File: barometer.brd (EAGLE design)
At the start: 58.4 x 40.4 mm, 95 parts, among them IC1 MIC5225-3.3v, IC2 TPS5410, IC3 ZPA2326-0311A-R, U1 MCP4725A0, U2 LTC2850, U3 PCA9306, U4 MAX3221, U5 XC6215XC6215B182NR, U6 Tiny85-20-SMT, X2 1751264, X3 1751248

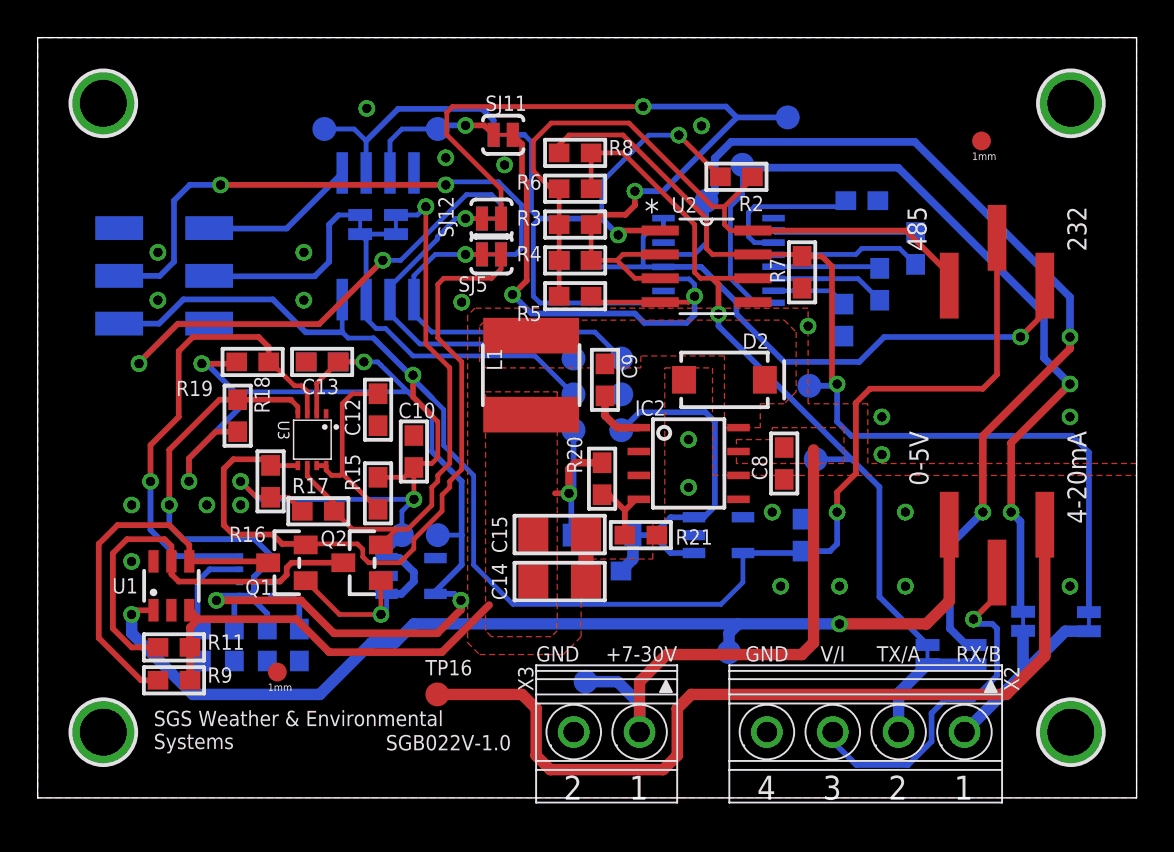
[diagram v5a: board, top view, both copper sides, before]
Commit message: Add 0-5 V to 4-20 mA converter
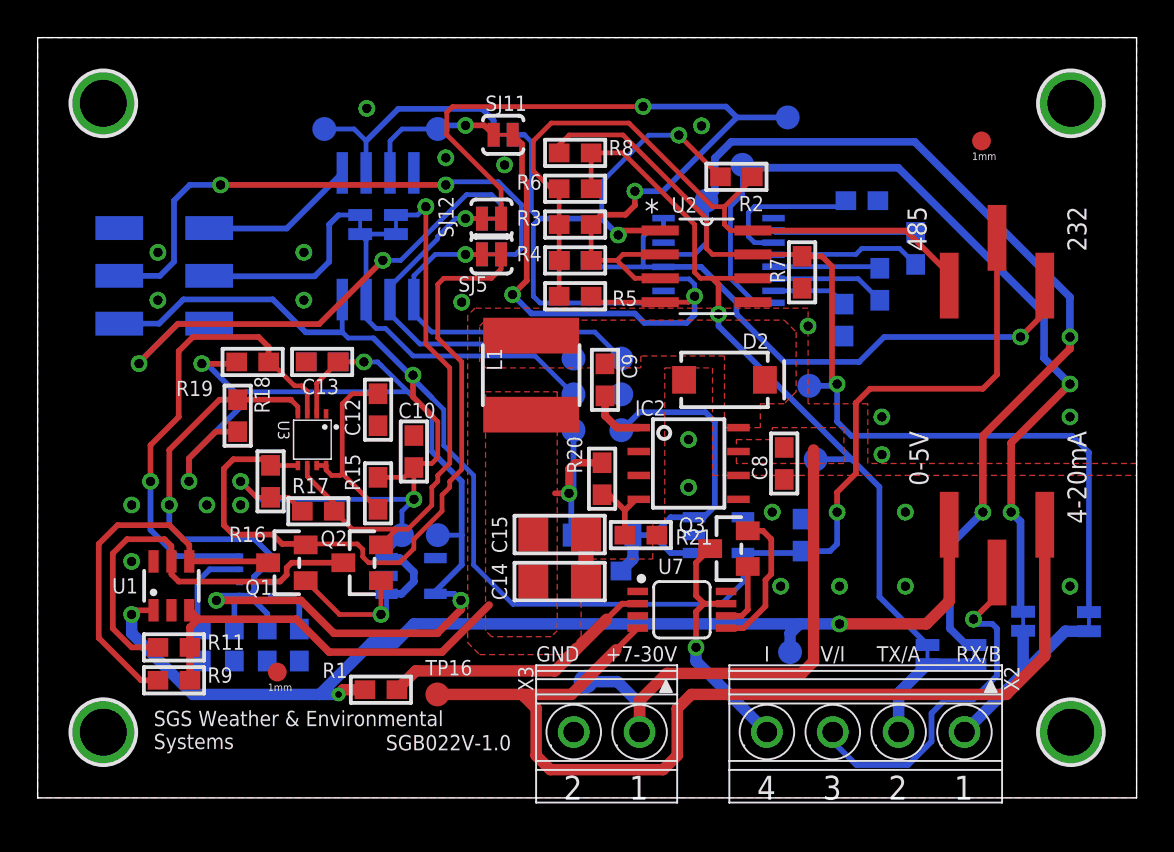
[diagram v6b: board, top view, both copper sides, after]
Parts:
- added Q3: BC817, microbuilder:SOT23-WIDE
- added R1: 25k, microbuilder:0603
- added U7: XTR117, transceiver-burrbrown:MSOP8-0.65-3X3MM
- moved TP15 3.25 mm to (40.0, 7.75)
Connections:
- new net BASE: Q3.1, U7.6
- new net COLLECTOR: Q3.3, U7.7, X2.4
- new net EMITTER: Q3.2, U7.5
- new net I-IN: R1.1, U7.2
- net GND: now also U7.3; no longer X2.4
- net I-OUT: now also U7.4
- net V-OUT: now also R1.2
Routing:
- net I-IN: track 0.00 -> 14.7 mm
- net COLLECTOR: track 0.00 -> 13.1 mm, vias 0 -> 1
- net EMITTER: track 0.00 -> 7.70 mm
- net I-OUT: track 46.4 -> 54.0 mm
- net BASE: track 0.00 -> 3.58 mm
- net V-OUT: track 54.9 -> 57.4 mm, vias 2 -> 3
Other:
- board text added: "I"
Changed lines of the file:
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@@
 <text x="34" y="7.25" size="0.8128" layer="25" font="vector" ratio="18" align="bottom-right">+7-30V</text>
 <text x="26.5" y="7.25" size="0.8128" layer="25" font="vector" ratio="18">GND</text>
-<text x="38.77" y="7.25" size="0.8128" layer="25" font="vector" ratio="18" align="bottom-center">GND</text>
+<text x="38.77" y="7.25" size="0.8128" layer="25" font="vector" ratio="18" align="bottom-center">I</text>
 <text x="51.23" y="7.25" size="0.8128" layer="25" font="vector" ratio="18" align="bottom-right">RX/B</text>
 <text x="45.77" y="7.25" size="0.8128" layer="25" font="vector" ratio="18" align="bottom-center">TX/A</text>
@@
 </element>
 <element name="R5" library="microbuilder" package="0603" value="10k" x="28.575" y="26.6675" smashed="yes" rot="R180">
-<attribute name="NAME" x="26.797" y="26.1595" size="0.8128" layer="25" font="vector" ratio="18" rot="R180"/>
+<attribute name="NAME" x="30.547" y="26.1595" size="0.8128" layer="25" font="vector" ratio="18"/>
 </element>
 <element name="R6" library="microbuilder" package="0603" value="20k" x="28.575" y="32.3825" smashed="yes" rot="R180">
@@
 <attribute name="NAME" x="23.7975" y="36.52" size="0.8128" layer="25" font="vector" ratio="18"/>
 </element>
-<element name="TP15" library="testpad" library_urn="urn:adsk.eagle:library:385" package="B1,27" package3d_urn="urn:adsk.eagle:package:27944/1" value="PTR1B1,27" x="36.75" y="7.75" smashed="yes" rot="MR0">
-<attribute name="NAME" x="38.385" y="8.766" size="0.8128" layer="26" font="vector" ratio="18" rot="MR0"/>
-<attribute name="TP_SIGNAL_NAME" value="" x="37.385" y="5.845" size="1" layer="38" rot="MR0"/>
+<element name="TP15" library="testpad" library_urn="urn:adsk.eagle:library:385" package="B1,27" package3d_urn="urn:adsk.eagle:package:27944/1" value="PTR1B1,27" x="40" y="7.75" smashed="yes" rot="MR0">
+<attribute name="NAME" x="41.635" y="8.766" size="0.8128" layer="26" font="vector" ratio="18" rot="MR0"/>
+<attribute name="TP_SIGNAL_NAME" value="" x="40.635" y="5.845" size="1" layer="38" rot="MR0"/>
 </element>
 <element name="TP16" library="testpad" library_urn="urn:adsk.eagle:library:385" package="B1,27" package3d_urn="urn:adsk.eagle:package:27944/1" value="PTR1B1,27" x="21.25" y="5.5" smashed="yes">
@@
 <attribute name="NAME" x="15.75" y="13.8" size="0.8128" layer="25" font="vector" ratio="18" rot="R180" align="center"/>
 <attribute name="VALUE" x="17.885" y="14.405" size="0.4064" layer="27" ratio="10" rot="R90"/>
+</element>
+<element name="U7" library="transceiver-burrbrown" package="MSOP8-0.65-3X3MM" value="XTR117" x="34.25" y="10" smashed="yes">
+<attribute name="NAME" x="32.98" y="11.905" size="0.8128" layer="25" font="vector" ratio="18"/>
+</element>
+<element name="R1" library="microbuilder" package="0603" value="25k" x="18.25" y="5.75" smashed="yes" rot="R180">
+<attribute name="NAME" x="16.472" y="6.377" size="0.8128" layer="25" font="vector" ratio="18" rot="R180" align="top-left"/>
+</element>
+<element name="Q3" library="microbuilder" package="SOT23-WIDE" value="BC817" x="36.75" y="13.25" smashed="yes" rot="R90">
+<attribute name="NAME" x="35.5" y="14.905" size="0.8128" layer="25" font="vector" ratio="18" rot="R180"/>
 </element>
 </elements>
@@
 <via x="5" y="15.57" extent="1-16" drill="0.5"/>
 <contactref element="X3" pad="2"/>
-<contactref element="X2" pad="4"/>
 <via x="10.795" y="15.57" extent="1-16" drill="0.5"/>
 <via x="14.1525" y="28.9975" extent="1-16" drill="0.5"/>
@@
 <via x="5" y="12.57" extent="1-16" drill="0.5"/>
 <via x="9" y="15.57" extent="1-16" drill="0.5"/>
+<contactref element="U7" pad="3"/>
 </signal>
 <signal name="+5V0">
@@
 <vertex x="37.1475" y="17.7775"/>
 </polygon>
-<wire x1="32" y1="6.1775" x2="33.44" y2="7.6175" width="0.6096" layer="1"/>
+<wire x1="32" y1="5.1775" x2="33.44" y2="6.6175" width="0.6096" layer="1"/>
 <contactref element="X3" pad="1"/>
-<wire x1="32" y1="6.1775" x2="32" y2="3.5" width="0.6096" layer="1"/>
-<wire x1="33.44" y1="7.6175" x2="40.6175" y2="7.6175" width="0.6096" layer="1"/>
-<wire x1="40.6175" y1="7.6175" x2="41.25" y2="8.25" width="0.6096" layer="1"/>
-<wire x1="41.25" y1="8.25" x2="41.25" y2="18.5" width="0.6096" layer="1"/>
+<wire x1="32" y1="5.1775" x2="32" y2="3.5" width="0.6096" layer="1"/>
+<wire x1="33.44" y1="6.6175" x2="40.6175" y2="6.6175" width="0.6096" layer="1"/>
+<wire x1="40.6175" y1="6.6175" x2="41.25" y2="7.25" width="0.6096" layer="1"/>
+<wire x1="41.25" y1="7.25" x2="41.25" y2="18.5" width="0.6096" layer="1"/>
 <wire x1="29.13" y1="6.18" x2="30.82" y2="6.18" width="0.6096" layer="16"/>
 <wire x1="30.82" y1="6.18" x2="32" y2="5" width="0.6096" layer="16"/>
@@
 <contactref element="TP15" pad="TP"/>
 <via x="42.63" y="9.25" extent="1-16" drill="0.5"/>
-<wire x1="42.63" y1="9.25" x2="37.25" y2="9.25" width="0.6096" layer="16"/>
-<wire x1="36.75" y1="7.75" x2="36.75" y2="8.75" width="0.6096" layer="16"/>
-<wire x1="36.75" y1="8.75" x2="37.25" y2="9.25" width="0.6096" layer="16"/>
+<wire x1="42.63" y1="9.25" x2="40.5" y2="9.25" width="0.6096" layer="16"/>
+<wire x1="40" y1="7.75" x2="40" y2="8.75" width="0.6096" layer="16"/>
+<wire x1="40" y1="8.75" x2="40.5" y2="9.25" width="0.6096" layer="16"/>
 <contactref element="JP1" pad="1"/>
 <wire x1="42.63" y1="9.25" x2="47.25" y2="9.25" width="0.6096" layer="1"/>
@@
 <wire x1="15" y1="5.5" x2="17.75" y2="8.25" width="0.6096" layer="16"/>
 <wire x1="17.75" y1="8.25" x2="19" y2="8.25" width="0.6096" layer="16"/>
-<wire x1="20" y1="9.25" x2="37.25" y2="9.25" width="0.6096" layer="16"/>
+<wire x1="20" y1="9.25" x2="40.5" y2="9.25" width="0.6096" layer="16"/>
+<contactref element="R1" pad="2"/>
+<wire x1="15" y1="5.5" x2="16" y2="5.5" width="0.6096" layer="16"/>
+<via x="16" y="5.5" extent="1-16" drill="0.35"/>
+<wire x1="16" y1="5.5" x2="16.25" y2="5.75" width="0.6096" layer="1"/>
+<wire x1="16.25" y1="5.75" x2="17.4" y2="5.75" width="0.6096" layer="1"/>
 </signal>
 <signal name="I-OUT">
@@
 <wire x1="51.5" y1="5.5" x2="53.54" y2="7.54" width="0.6096" layer="1"/>
 <wire x1="53.54" y1="7.54" x2="53.54" y2="14.52" width="0.6096" layer="1"/>
+<contactref element="U7" pad="4"/>
+<wire x1="25.75" y1="5.5" x2="28.375" y2="5.5" width="0.6096" layer="1"/>
+<wire x1="30.75" y1="7.875" x2="31.9" y2="9.025" width="0.3048" layer="1"/>
+<wire x1="28.375" y1="5.5" x2="30.75" y2="7.875" width="0.6096" layer="1"/>
 </signal>
 <signal name="SDA_5V0">
@@
 <wire x1="4" y1="9" x2="4" y2="13" width="0.3048" layer="1"/>
 </signal>
+<signal name="I-IN">
+<contactref element="R1" pad="1"/>
+<contactref element="U7" pad="2"/>
+<wire x1="19.1" y1="5.75" x2="20.1" y2="6.75" width="0.6096" layer="1"/>
+<wire x1="20.1" y1="6.75" x2="27.5" y2="6.75" width="0.6096" layer="1"/>
+<wire x1="27.5" y1="6.75" x2="30.25" y2="9.5" width="0.6096" layer="1"/>
+<wire x1="30.25" y1="9.5" x2="31.075" y2="10.325" width="0.3048" layer="1"/>
+<wire x1="31.075" y1="10.325" x2="31.9" y2="10.325" width="0.3048" layer="1"/>
+</signal>
+<signal name="EMITTER">
+<contactref element="U7" pad="5"/>
+<contactref element="Q3" pad="2"/>
+<wire x1="37.75" y1="14.2" x2="38.55" y2="14.2" width="0.3048" layer="1"/>
+<wire x1="38.55" y1="14.2" x2="39" y2="13.75" width="0.3048" layer="1"/>
+<wire x1="39" y1="11.89631875" x2="38.6912" y2="11.58751875" width="0.3048" layer="1"/>
+<wire x1="39" y1="13.75" x2="39" y2="11.89631875" width="0.3048" layer="1"/>
+<wire x1="38.6912" y1="10.1912" x2="38.6912" y2="11.58751875" width="0.3048" layer="1"/>
+<wire x1="37.525" y1="9.025" x2="38.6912" y2="10.1912" width="0.3048" layer="1"/>
+<wire x1="36.6" y1="9.025" x2="37.525" y2="9.025" width="0.3048" layer="1"/>
+</signal>
+<signal name="COLLECTOR">
+<contactref element="U7" pad="7"/>
+<contactref element="Q3" pad="3"/>
+<contactref element="X2" pad="4"/>
+<wire x1="35.75" y1="13.25" x2="35" y2="12.5" width="0.3048" layer="1"/>
+<wire x1="35" y1="10.75" x2="35.425" y2="10.325" width="0.3048" layer="1"/>
+<wire x1="35.425" y1="10.325" x2="36.6" y2="10.325" width="0.3048" layer="1"/>
+<wire x1="35" y1="12.5" x2="35" y2="10.75" width="0.3048" layer="1"/>
+<wire x1="38.77" y1="3.5" x2="35" y2="7.27" width="0.6096" layer="16"/>
+<via x="35" y="8" extent="1-16" drill="0.5"/>
+<wire x1="35" y1="8" x2="35" y2="9.9" width="0.3048" layer="1"/>
+<wire x1="35" y1="9.9" x2="35.425" y2="10.325" width="0.3048" layer="1"/>
+<wire x1="35" y1="7.27" x2="35" y2="8" width="0.6096" layer="16"/>
+</signal>
+<signal name="BASE">
+<contactref element="U7" pad="6"/>
+<contactref element="Q3" pad="1"/>
+<wire x1="37.75" y1="12.3" x2="37.75" y2="10" width="0.3048" layer="1"/>
+<wire x1="37.425" y1="9.675" x2="36.6" y2="9.675" width="0.3048" layer="1"/>
+<wire x1="37.75" y1="10" x2="37.425" y2="9.675" width="0.3048" layer="1"/>
+</signal>
 </signals>
